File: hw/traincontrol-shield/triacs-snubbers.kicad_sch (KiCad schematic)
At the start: 6 parts, among them Q1 BT134W-600D, Q2 BT134W-600D

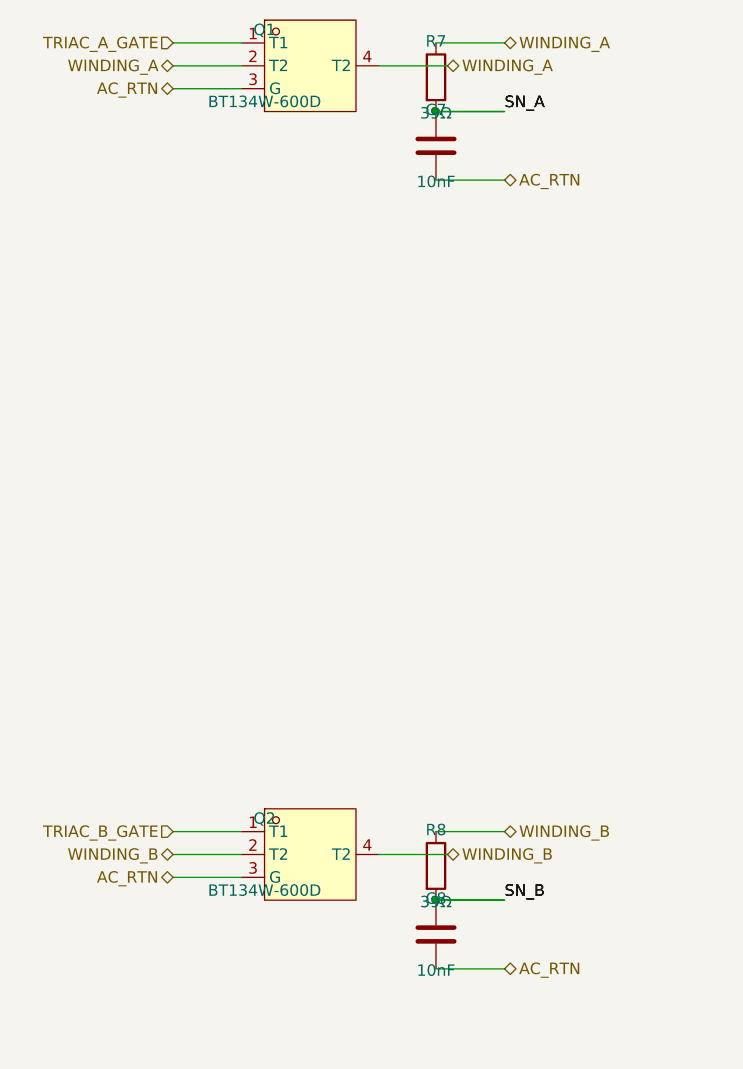
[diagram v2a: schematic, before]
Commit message: Increase component spacing to eliminate pin-wire overlaps
- zero-crossing: move R1 left 7.62mm, add bridge wire to U2 pin2
- xor-interlock: move C10 right of U3 output (76→91mm), move C11 right (168→178mm)
- opto-triac: add 7.62mm COMP_GAP between MOC3021 and LED/gate resistors
- triacs-snubbers: move snubber column right (99→109mm), add 7.62mm gap between R and C
- mcu: widen C4/C5/C6 decap spacing from 7.62mm to 10.16mm
- power-supply: move R13 down 7.62mm, add bridge wire to R12

Co-Authored-By: Claude Sonnet 4.6 <noreply@anthropic.com>
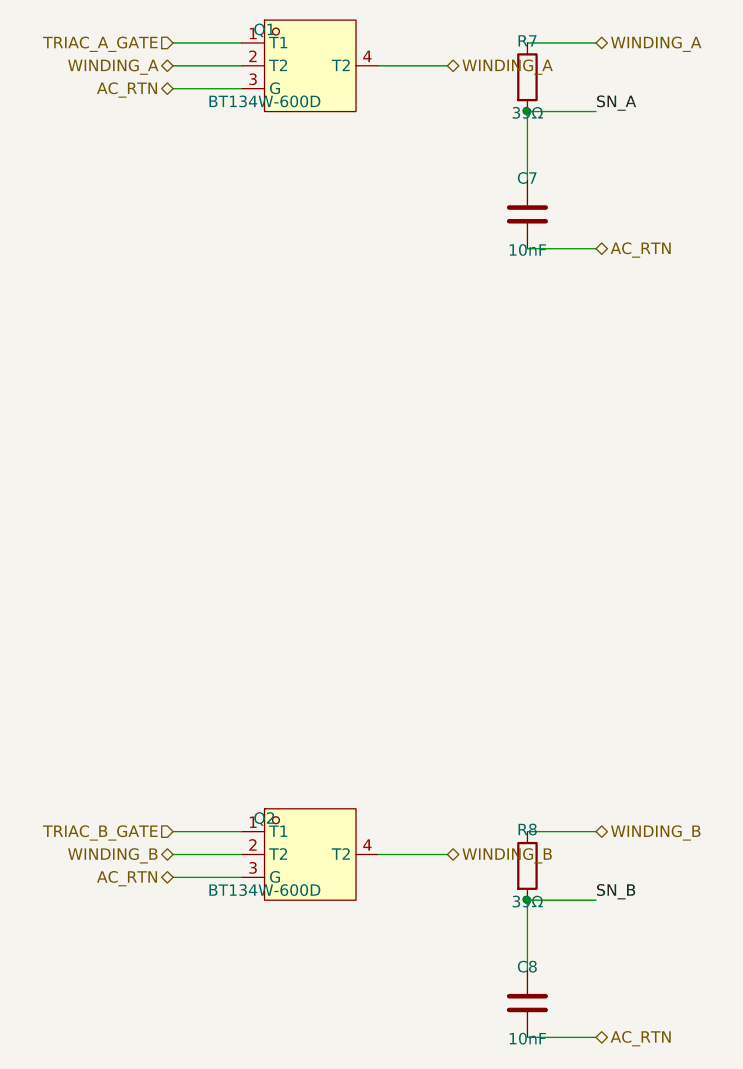
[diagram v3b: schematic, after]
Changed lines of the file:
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@@
 	(symbol
 		(lib_id "Device:R")
-		(at 99.06 91.44 0)
+		(at 109.22 91.44 0)
 		(unit 1)
 		(exclude_from_sim no)
@@
 		(dnp no)
 		(property "Reference" "R7"
-			(at 99.06 87.44 0)
+			(at 109.22 87.44 0)
 			(effects (font (size 1.27 1.27)))
 		)
 		(property "Value" "39Ω"
-			(at 99.06 95.44 0)
+			(at 109.22 95.44 0)
 			(effects (font (size 1.27 1.27)))
 		)
 		(property "Footprint" "Resistor_SMD:R_0603_1608Metric"
-			(at 99.06 91.44 0)
-			(effects (font (size 1.27 1.27)) (hide yes))
-		)
-		(property "Datasheet" "~"
-			(at 99.06 91.44 0)
+			(at 109.22 91.44 0)
+			(effects (font (size 1.27 1.27)) (hide yes))
+		)
+		(property "Datasheet" "~"
+			(at 109.22 91.44 0)
 			(effects (font (size 1.27 1.27)) (hide yes))
 		)
@@
 	)
 	(wire
-		(pts (xy 99.06 87.63) (xy 106.68 87.63))
+		(pts (xy 109.22 87.63) (xy 116.84 87.63))
 		(stroke (width 0) (type solid))
 	)
 	(hierarchical_label "WINDING_A"
 		(shape bidirectional)
-		(at 106.68 87.63 0)
-		(fields_autoplaced yes)
-		(effects (font (size 1.27 1.27)) (justify left bottom))
-		(property "Intersheetrefs" "${INTERSHEET_REFS}"
-			(at 106.68 87.63 0)
-			(effects (font (size 1.27 1.27)) (hide yes))
-		)
-	)
-	(wire
-		(pts (xy 99.06 95.25) (xy 106.68 95.25))
+		(at 116.84 87.63 0)
+		(fields_autoplaced yes)
+		(effects (font (size 1.27 1.27)) (justify left bottom))
+		(property "Intersheetrefs" "${INTERSHEET_REFS}"
+			(at 116.84 87.63 0)
+			(effects (font (size 1.27 1.27)) (hide yes))
+		)
+	)
+	(wire
+		(pts (xy 109.22 95.25) (xy 116.84 95.25))
 		(stroke (width 0) (type solid))
 	)
 	(label "SN_A"
-		(at 106.68 95.25 0)
-		(fields_autoplaced yes)
-		(effects (font (size 1.27 1.27)) (justify left bottom))
+		(at 116.84 95.25 0)
+		(fields_autoplaced yes)
+		(effects (font (size 1.27 1.27)) (justify left bottom))
+	)
+	(wire
+		(pts (xy 109.22 95.25) (xy 109.22 102.87))
+		(stroke (width 0) (type solid))
 	)
 	(symbol
 		(lib_id "Device:C")
-		(at 99.06 99.06 0)
+		(at 109.22 106.68 0)
 		(unit 1)
 		(exclude_from_sim no)
@@
 		(dnp no)
 		(property "Reference" "C7"
-			(at 99.06 95.06 0)
+			(at 109.22 102.68 0)
 			(effects (font (size 1.27 1.27)))
 		)
 		(property "Value" "10nF"
-			(at 99.06 103.06 0)
+			(at 109.22 110.68 0)
 			(effects (font (size 1.27 1.27)))
 		)
 		(property "Footprint" "Capacitor_SMD:C_0603_1608Metric"
-			(at 99.06 99.06 0)
-			(effects (font (size 1.27 1.27)) (hide yes))
-		)
-		(property "Datasheet" "~"
-			(at 99.06 99.06 0)
+			(at 109.22 106.68 0)
+			(effects (font (size 1.27 1.27)) (hide yes))
+		)
+		(property "Datasheet" "~"
+			(at 109.22 106.68 0)
 			(effects (font (size 1.27 1.27)) (hide yes))
 		)
@@
 	)
 	(wire
-		(pts (xy 99.06 95.25) (xy 106.68 95.25))
-		(stroke (width 0) (type solid))
-	)
-	(label "SN_A"
-		(at 106.68 95.25 0)
-		(fields_autoplaced yes)
-		(effects (font (size 1.27 1.27)) (justify left bottom))
-	)
-	(wire
-		(pts (xy 99.06 102.87) (xy 106.68 102.87))
+		(pts (xy 109.22 110.49000000000001) (xy 116.84 110.49000000000001))
 		(stroke (width 0) (type solid))
 	)
 	(hierarchical_label "AC_RTN"
 		(shape bidirectional)
-		(at 106.68 102.87 0)
-		(fields_autoplaced yes)
-		(effects (font (size 1.27 1.27)) (justify left bottom))
-		(property "Intersheetrefs" "${INTERSHEET_REFS}"
-			(at 106.68 102.87 0)
+		(at 116.84 110.49000000000001 0)
+		(fields_autoplaced yes)
+		(effects (font (size 1.27 1.27)) (justify left bottom))
+		(property "Intersheetrefs" "${INTERSHEET_REFS}"
+			(at 116.84 110.49000000000001 0)
 			(effects (font (size 1.27 1.27)) (hide yes))
 		)
 	)
 	(junction
-		(at 99.06 95.25)
+		(at 109.22 95.25)
 		(diameter 0)
 		(color 0 0 0 0)
@@
 	(symbol
 		(lib_id "Device:R")
-		(at 99.06 179.07000000000002 0)
+		(at 109.22 179.07000000000002 0)
 		(unit 1)
 		(exclude_from_sim no)
@@
 		(dnp no)
 		(property "Reference" "R8"
-			(at 99.06 175.07000000000002 0)
+			(at 109.22 175.07000000000002 0)
 			(effects (font (size 1.27 1.27)))
 		)
 		(property "Value" "39Ω"
-			(at 99.06 183.07000000000002 0)
+			(at 109.22 183.07000000000002 0)
 			(effects (font (size 1.27 1.27)))
 		)
 		(property "Footprint" "Resistor_SMD:R_0603_1608Metric"
-			(at 99.06 179.07000000000002 0)
-			(effects (font (size 1.27 1.27)) (hide yes))
-		)
-		(property "Datasheet" "~"
-			(at 99.06 179.07000000000002 0)
+			(at 109.22 179.07000000000002 0)
+			(effects (font (size 1.27 1.27)) (hide yes))
+		)
+		(property "Datasheet" "~"
+			(at 109.22 179.07000000000002 0)
 			(effects (font (size 1.27 1.27)) (hide yes))
 		)
@@
 	)
 	(wire
-		(pts (xy 99.06 175.26000000000002) (xy 106.68 175.26000000000002))
+		(pts (xy 109.22 175.26000000000002) (xy 116.84 175.26000000000002))
 		(stroke (width 0) (type solid))
 	)
 	(hierarchical_label "WINDING_B"
 		(shape bidirectional)
-		(at 106.68 175.26000000000002 0)
-		(fields_autoplaced yes)
-		(effects (font (size 1.27 1.27)) (justify left bottom))
-		(property "Intersheetrefs" "${INTERSHEET_REFS}"
-			(at 106.68 175.26000000000002 0)
-			(effects (font (size 1.27 1.27)) (hide yes))
-		)
-	)
-	(wire
-		(pts (xy 99.06 182.88000000000002) (xy 106.68 182.88000000000002))
+		(at 116.84 175.26000000000002 0)
+		(fields_autoplaced yes)
+		(effects (font (size 1.27 1.27)) (justify left bottom))
+		(property "Intersheetrefs" "${INTERSHEET_REFS}"
+			(at 116.84 175.26000000000002 0)
+			(effects (font (size 1.27 1.27)) (hide yes))
+		)
+	)
+	(wire
+		(pts (xy 109.22 182.88000000000002) (xy 116.84 182.88000000000002))
 		(stroke (width 0) (type solid))
 	)
 	(label "SN_B"
-		(at 106.68 182.88000000000002 0)
-		(fields_autoplaced yes)
-		(effects (font (size 1.27 1.27)) (justify left bottom))
+		(at 116.84 182.88000000000002 0)
+		(fields_autoplaced yes)
+		(effects (font (size 1.27 1.27)) (justify left bottom))
+	)
+	(wire
+		(pts (xy 109.22 182.88000000000002) (xy 109.22 190.50000000000003))
+		(stroke (width 0) (type solid))
 	)
 	(symbol
 		(lib_id "Device:C")
-		(at 99.06 186.69000000000003 0)
+		(at 109.22 194.31000000000003 0)
 		(unit 1)
 		(exclude_from_sim no)
@@
 		(dnp no)
 		(property "Reference" "C8"
-			(at 99.06 182.69000000000003 0)
+			(at 109.22 190.31000000000003 0)
 			(effects (font (size 1.27 1.27)))
 		)
 		(property "Value" "10nF"
-			(at 99.06 190.69000000000003 0)
+			(at 109.22 198.31000000000003 0)
 			(effects (font (size 1.27 1.27)))
 		)
 		(property "Footprint" "Capacitor_SMD:C_0603_1608Metric"
-			(at 99.06 186.69000000000003 0)
-			(effects (font (size 1.27 1.27)) (hide yes))
-		)
-		(property "Datasheet" "~"
-			(at 99.06 186.69000000000003 0)
+			(at 109.22 194.31000000000003 0)
+			(effects (font (size 1.27 1.27)) (hide yes))
+		)
+		(property "Datasheet" "~"
+			(at 109.22 194.31000000000003 0)
 			(effects (font (size 1.27 1.27)) (hide yes))
 		)
@@
 	)
 	(wire
-		(pts (xy 99.06 182.88000000000002) (xy 106.68 182.88000000000002))
-		(stroke (width 0) (type solid))
-	)
-	(label "SN_B"
-		(at 106.68 182.88000000000002 0)
-		(fields_autoplaced yes)
-		(effects (font (size 1.27 1.27)) (justify left bottom))
-	)
-	(wire
-		(pts (xy 99.06 190.50000000000003) (xy 106.68 190.50000000000003))
+		(pts (xy 109.22 198.12000000000003) (xy 116.84 198.12000000000003))
 		(stroke (width 0) (type solid))
 	)
 	(hierarchical_label "AC_RTN"
 		(shape bidirectional)
-		(at 106.68 190.50000000000003 0)
-		(fields_autoplaced yes)
-		(effects (font (size 1.27 1.27)) (justify left bottom))
-		(property "Intersheetrefs" "${INTERSHEET_REFS}"
-			(at 106.68 190.50000000000003 0)
+		(at 116.84 198.12000000000003 0)
+		(fields_autoplaced yes)
+		(effects (font (size 1.27 1.27)) (justify left bottom))
+		(property "Intersheetrefs" "${INTERSHEET_REFS}"
+			(at 116.84 198.12000000000003 0)
 			(effects (font (size 1.27 1.27)) (hide yes))
 		)
 	)
 	(junction
-		(at 99.06 182.88000000000002)
+		(at 109.22 182.88000000000002)
 		(diameter 0)
 		(color 0 0 0 0)

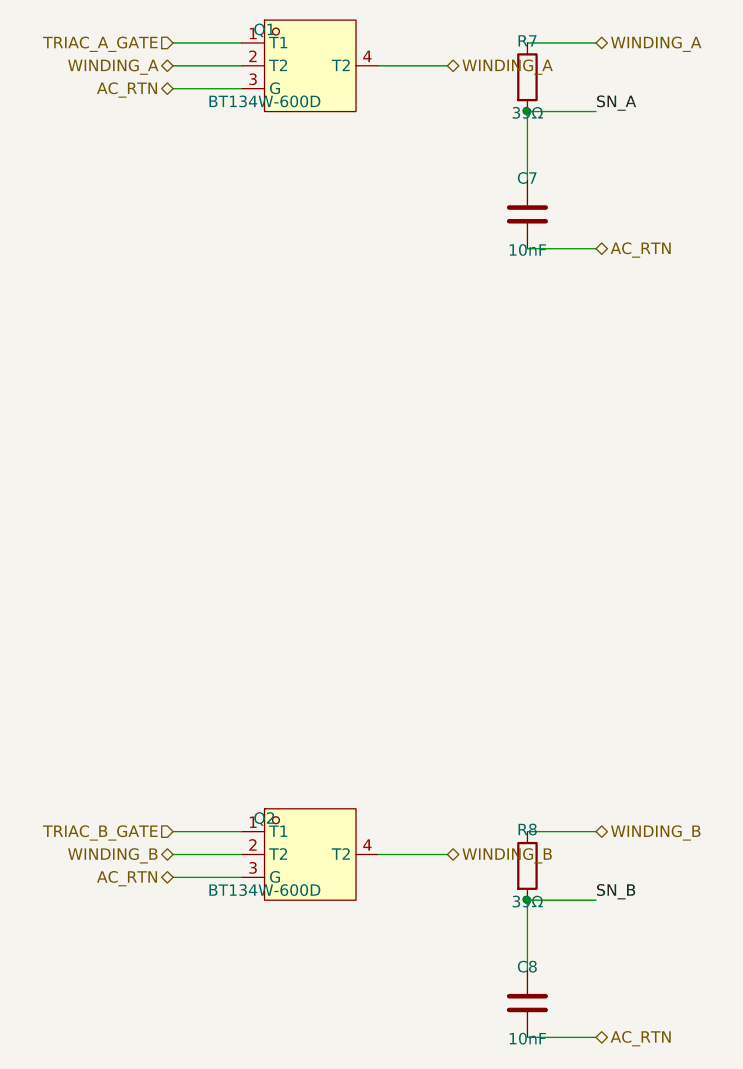
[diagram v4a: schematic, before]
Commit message: Fix schematic ERC errors: pin Y-flip, PWR_FLAG, label wiring, spacing
- Fix connector pin positions using Y-flip convention (sym Y-up → sch Y-down)
- Add GND PWR_FLAG to power-supply sheet (eliminates power_pin_not_driven)
- Fix top-level connector label placement: labels at stub end, wires toward pins
- Apply omnidirectional spacing and IC-to-passive body gap rules across sheets
- Update schematics-plan.md with ERC workflow and coordinate conventions
- Regenerate all sub-sheets with corrected generator scripts

ERC result: 138 violations (all warnings/cosmetic), 0 critical errors.

Co-Authored-By: Claude Opus 4.6 <noreply@anthropic.com>
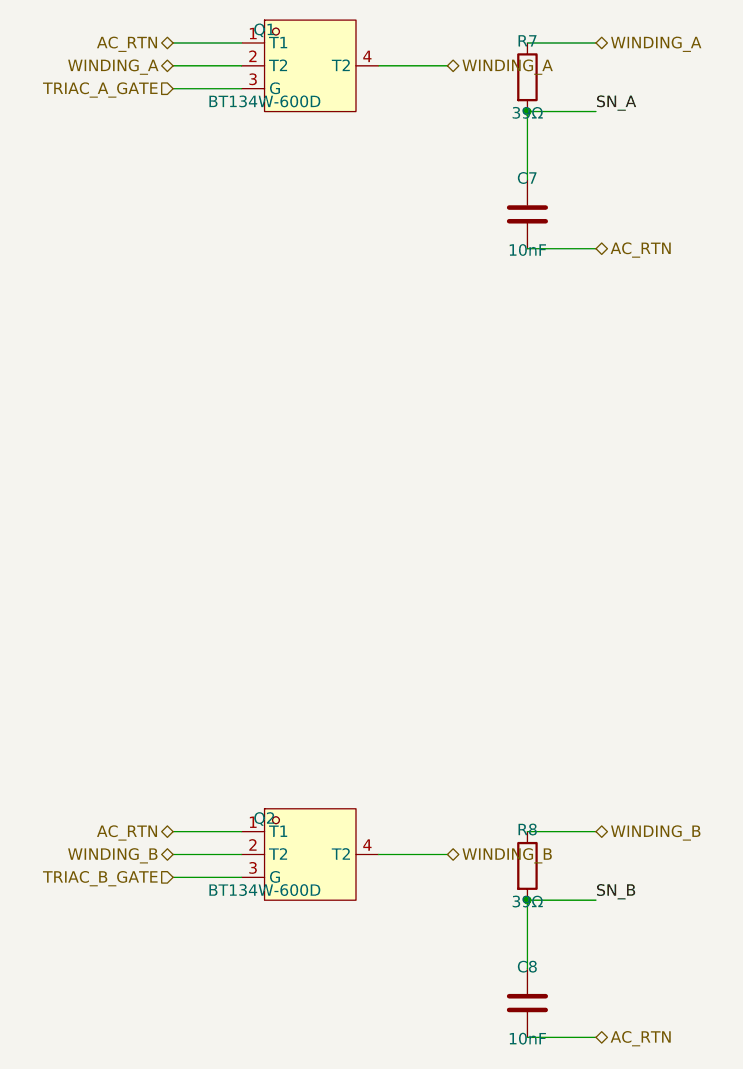
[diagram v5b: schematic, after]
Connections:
- net AC_RTN: now also Q1.1 (T1), Q2.1 (T1); no longer Q1.3 (G), Q2.3 (G)
- net TRIAC_A_GATE: now also Q1.3 (G); no longer Q1.1 (T1)
- net TRIAC_B_GATE: now also Q2.3 (G); no longer Q2.1 (T1)
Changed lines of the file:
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@@
+	)
+	(wire
+		(pts (xy 69.85 87.63) (xy 77.47 87.63))
+		(stroke (width 0) (type solid))
+	)
+	(hierarchical_label "AC_RTN"
+		(shape bidirectional)
+		(at 69.85 87.63 180)
+		(fields_autoplaced yes)
+		(effects (font (size 1.27 1.27)) (justify right bottom))
+		(property "Intersheetrefs" "${INTERSHEET_REFS}"
+			(at 69.85 87.63 0)
+			(effects (font (size 1.27 1.27)) (hide yes))
+		)
+	)
+	(wire
+		(pts (xy 69.85 90.17) (xy 77.47 90.17))
+		(stroke (width 0) (type solid))
+	)
+	(hierarchical_label "WINDING_A"
+		(shape bidirectional)
+		(at 69.85 90.17 180)
+		(fields_autoplaced yes)
+		(effects (font (size 1.27 1.27)) (justify right bottom))
+		(property "Intersheetrefs" "${INTERSHEET_REFS}"
+			(at 69.85 90.17 0)
+			(effects (font (size 1.27 1.27)) (hide yes))
+		)
+	)
+	(wire
+		(pts (xy 92.71000000000001 90.17) (xy 100.33000000000001 90.17))
+		(stroke (width 0) (type solid))
+	)
+	(hierarchical_label "WINDING_A"
+		(shape bidirectional)
+		(at 100.33000000000001 90.17 0)
+		(fields_autoplaced yes)
+		(effects (font (size 1.27 1.27)) (justify left bottom))
+		(property "Intersheetrefs" "${INTERSHEET_REFS}"
+			(at 100.33000000000001 90.17 0)
+			(effects (font (size 1.27 1.27)) (hide yes))
+		)
 	)
 	(wire
 		(pts (xy 69.85 92.71000000000001) (xy 77.47 92.71000000000001))
-		(stroke (width 0) (type solid))
-	)
-	(hierarchical_label "AC_RTN"
-		(shape bidirectional)
-		(at 69.85 92.71000000000001 180)
-		(fields_autoplaced yes)
-		(effects (font (size 1.27 1.27)) (justify right bottom))
-		(property "Intersheetrefs" "${INTERSHEET_REFS}"
-			(at 69.85 92.71000000000001 0)
-			(effects (font (size 1.27 1.27)) (hide yes))
-		)
-	)
-	(wire
-		(pts (xy 69.85 90.17) (xy 77.47 90.17))
-		(stroke (width 0) (type solid))
-	)
-	(hierarchical_label "WINDING_A"
-		(shape bidirectional)
-		(at 69.85 90.17 180)
-		(fields_autoplaced yes)
-		(effects (font (size 1.27 1.27)) (justify right bottom))
-		(property "Intersheetrefs" "${INTERSHEET_REFS}"
-			(at 69.85 90.17 0)
-			(effects (font (size 1.27 1.27)) (hide yes))
-		)
-	)
-	(wire
-		(pts (xy 92.71000000000001 90.17) (xy 100.33000000000001 90.17))
-		(stroke (width 0) (type solid))
-	)
-	(hierarchical_label "WINDING_A"
-		(shape bidirectional)
-		(at 100.33000000000001 90.17 0)
-		(fields_autoplaced yes)
-		(effects (font (size 1.27 1.27)) (justify left bottom))
-		(property "Intersheetrefs" "${INTERSHEET_REFS}"
-			(at 100.33000000000001 90.17 0)
-			(effects (font (size 1.27 1.27)) (hide yes))
-		)
-	)
-	(wire
-		(pts (xy 69.85 87.63) (xy 77.47 87.63))
 		(stroke (width 0) (type solid))
 	)
 	(hierarchical_label "TRIAC_A_GATE"
 		(shape input)
-		(at 69.85 87.63 180)
-		(fields_autoplaced yes)
-		(effects (font (size 1.27 1.27)) (justify right bottom))
-		(property "Intersheetrefs" "${INTERSHEET_REFS}"
-			(at 69.85 87.63 0)
+		(at 69.85 92.71000000000001 180)
+		(fields_autoplaced yes)
+		(effects (font (size 1.27 1.27)) (justify right bottom))
+		(property "Intersheetrefs" "${INTERSHEET_REFS}"
+			(at 69.85 92.71000000000001 0)
 			(effects (font (size 1.27 1.27)) (hide yes))
 		)
@@
 	)
 	(wire
+		(pts (xy 69.85 175.26000000000002) (xy 77.47 175.26000000000002))
+		(stroke (width 0) (type solid))
+	)
+	(hierarchical_label "AC_RTN"
+		(shape bidirectional)
+		(at 69.85 175.26000000000002 180)
+		(fields_autoplaced yes)
+		(effects (font (size 1.27 1.27)) (justify right bottom))
+		(property "Intersheetrefs" "${INTERSHEET_REFS}"
+			(at 69.85 175.26000000000002 0)
+			(effects (font (size 1.27 1.27)) (hide yes))
+		)
+	)
+	(wire
+		(pts (xy 69.85 177.8) (xy 77.47 177.8))
+		(stroke (width 0) (type solid))
+	)
+	(hierarchical_label "WINDING_B"
+		(shape bidirectional)
+		(at 69.85 177.8 180)
+		(fields_autoplaced yes)
+		(effects (font (size 1.27 1.27)) (justify right bottom))
+		(property "Intersheetrefs" "${INTERSHEET_REFS}"
+			(at 69.85 177.8 0)
+			(effects (font (size 1.27 1.27)) (hide yes))
+		)
+	)
+	(wire
+		(pts (xy 92.71000000000001 177.8) (xy 100.33000000000001 177.8))
+		(stroke (width 0) (type solid))
+	)
+	(hierarchical_label "WINDING_B"
+		(shape bidirectional)
+		(at 100.33000000000001 177.8 0)
+		(fields_autoplaced yes)
+		(effects (font (size 1.27 1.27)) (justify left bottom))
+		(property "Intersheetrefs" "${INTERSHEET_REFS}"
+			(at 100.33000000000001 177.8 0)
+			(effects (font (size 1.27 1.27)) (hide yes))
+		)
+	)
+	(wire
 		(pts (xy 69.85 180.34) (xy 77.47 180.34))
-		(stroke (width 0) (type solid))
-	)
-	(hierarchical_label "AC_RTN"
-		(shape bidirectional)
-		(at 69.85 180.34 180)
-		(fields_autoplaced yes)
-		(effects (font (size 1.27 1.27)) (justify right bottom))
-		(property "Intersheetrefs" "${INTERSHEET_REFS}"
-			(at 69.85 180.34 0)
-			(effects (font (size 1.27 1.27)) (hide yes))
-		)
-	)
-	(wire
-		(pts (xy 69.85 177.8) (xy 77.47 177.8))
-		(stroke (width 0) (type solid))
-	)
-	(hierarchical_label "WINDING_B"
-		(shape bidirectional)
-		(at 69.85 177.8 180)
-		(fields_autoplaced yes)
-		(effects (font (size 1.27 1.27)) (justify right bottom))
-		(property "Intersheetrefs" "${INTERSHEET_REFS}"
-			(at 69.85 177.8 0)
-			(effects (font (size 1.27 1.27)) (hide yes))
-		)
-	)
-	(wire
-		(pts (xy 92.71000000000001 177.8) (xy 100.33000000000001 177.8))
-		(stroke (width 0) (type solid))
-	)
-	(hierarchical_label "WINDING_B"
-		(shape bidirectional)
-		(at 100.33000000000001 177.8 0)
-		(fields_autoplaced yes)
-		(effects (font (size 1.27 1.27)) (justify left bottom))
-		(property "Intersheetrefs" "${INTERSHEET_REFS}"
-			(at 100.33000000000001 177.8 0)
-			(effects (font (size 1.27 1.27)) (hide yes))
-		)
-	)
-	(wire
-		(pts (xy 69.85 175.26000000000002) (xy 77.47 175.26000000000002))
 		(stroke (width 0) (type solid))
 	)
 	(hierarchical_label "TRIAC_B_GATE"
 		(shape input)
-		(at 69.85 175.26000000000002 180)
-		(fields_autoplaced yes)
-		(effects (font (size 1.27 1.27)) (justify right bottom))
-		(property "Intersheetrefs" "${INTERSHEET_REFS}"
-			(at 69.85 175.26000000000002 0)
-			(effects (font (size 1.27 1.27)) (hide yes))
-		)
+		(at 69.85 180.34 180)
+		(fields_autoplaced yes)
+		(effects (font (size 1.27 1.27)) (justify right bottom))
+		(property "Intersheetrefs" "${INTERSHEET_REFS}"
+			(at 69.85 180.34 0)
+			(effects (font (size 1.27 1.27)) (hide yes))
+		)
